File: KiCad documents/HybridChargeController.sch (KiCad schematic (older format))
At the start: 89 parts

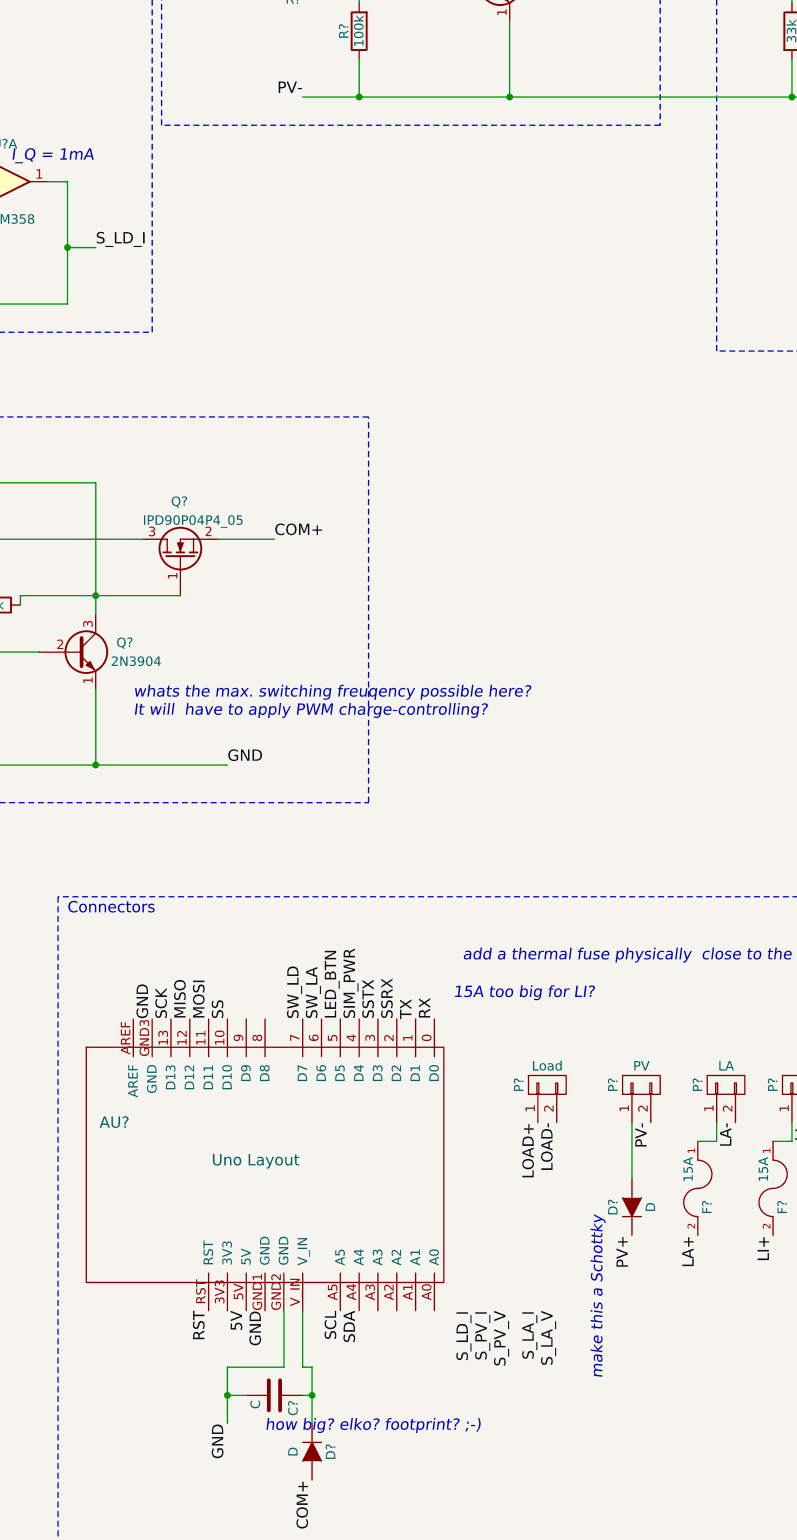
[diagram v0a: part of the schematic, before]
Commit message: added multiplexer
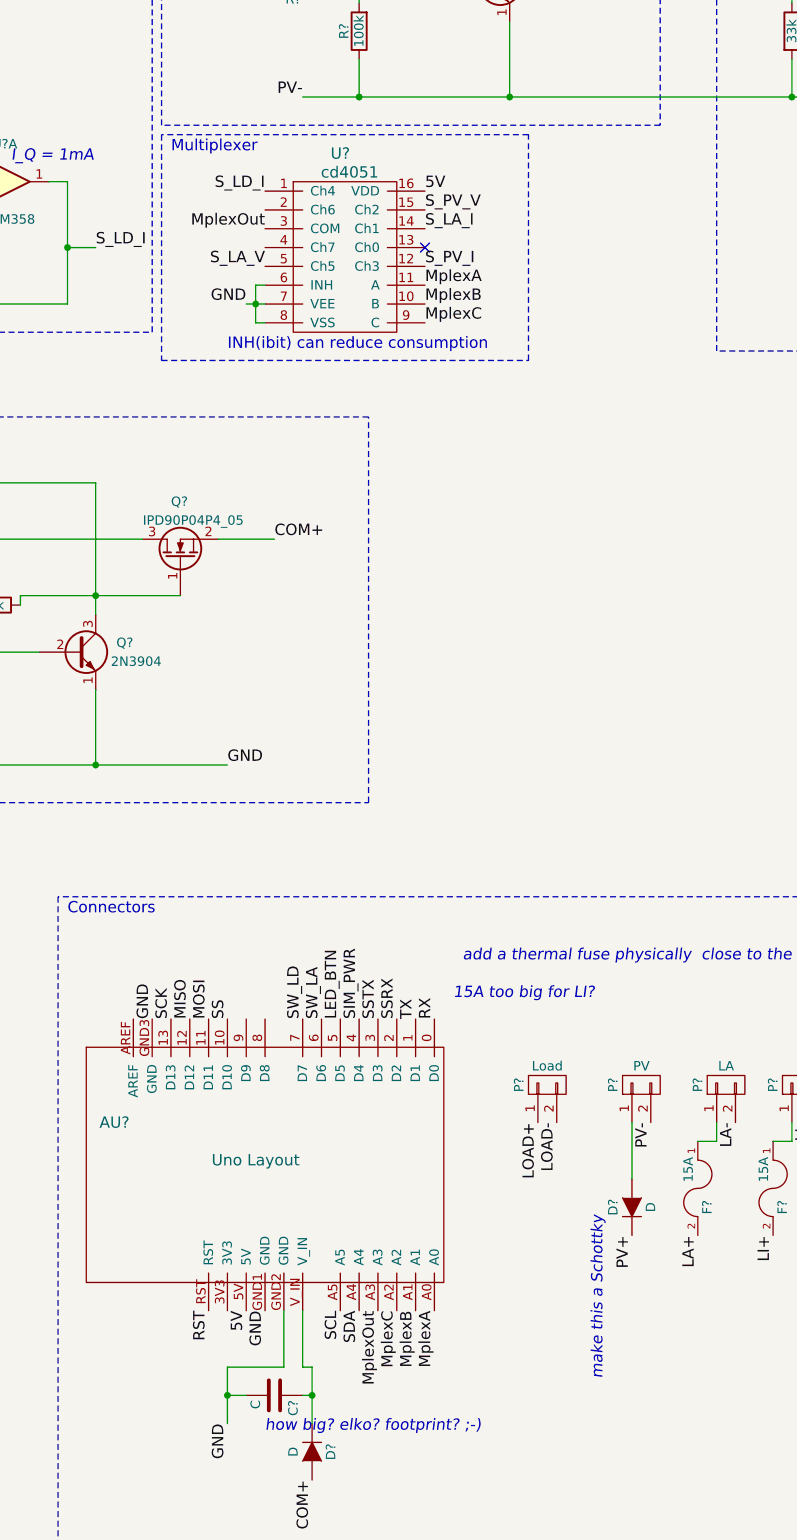
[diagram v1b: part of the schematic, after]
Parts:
- added U?: cd4051, symbol cd4051
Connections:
- net 5V: now also U?.16 (VDD)
- net GND: now also U?.6 (INH), U?.7 (VEE), U?.8 (VSS)
- net S_LA_I: now also U?.14 (Ch1)
- net S_LA_V: now also U?.5 (Ch5)
- net S_LD_I: now also U?.1 (Ch4)
- net S_PV_I: now also U?.12 (Ch3)
- net S_PV_V: now also U?.15 (Ch2)
- net MplexA: now reaches AU?.A0
- net MplexA: now also U?.11 (A)
- net MplexB: now reaches AU?.A1
- net MplexB: now also U?.10 (B)
- net MplexC: now reaches AU?.A2
- net MplexC: now also U?.9 (C)
- net MplexOut: now reaches AU?.A3
- net MplexOut: now also U?.3 (COM)
- no-connect marks 1 -> 2
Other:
- note added: "INH(ibit) can reduce consumption"
- note added: "Multiplexer"
- note removed: "whats the max. switching freuqency possible here? \nIt will have to apply PWM charge-controlling?"

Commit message: added protections
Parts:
- added D? (x2): D, symbol D
- added Q? (x2): Q_PMOS_DGS, symbol Q_PMOS_DGS
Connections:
- wire segments 258 -> 282
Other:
- note added: "10mF?"
- note added: "Connectors & Protection"
- note added: "OR BALANCER"
- note added: "Schottky"
- note added: "protection: \nreverse polarity & short circuit"
- note removed: "15A too big for LI?"
- note removed: "Connectors"
- note removed: "how big? elko? footprint? ;-)"
- note removed: "make this a Schottky"
- moved on the sheet: D?, F?, P?

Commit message: selfmade STL60P4LLF6
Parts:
- removed D? (x2): D, symbol D
- removed F?: 15A, symbol FUSE
- removed P?: LI, symbol CONN_01X02
- removed Q? (x2): Q_PMOS_DGS, symbol Q_PMOS_DGS
- added F?: 15A, symbol FUSE
- added P?: LI, symbol CONN_01X02
- added Q? (x2): STL60P4LLF6, symbol STL60P4LLF6
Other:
- note removed: "OR BALANCER"
- moved on the sheet: F?, P?

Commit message: order ready
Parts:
- removed C? (x3): Cc, symbol C_Small
- removed D? (x2): D, symbol D
- removed D?: ZENER, symbol ZENER
- removed Q?: N FET cheap, symbol Q_NMOS_DGS
- removed R? (x4): Rc, symbol R
- added C2, C3, C4: 1µ, symbol C_Small
- added P4: Extra, symbol CONN_01X07
- added Q4: BSS138, TO_SOT_Packages_SMD:SOT-23, symbol BSS138
- added R2, R3, R4, R5: 100, symbol R
- C1: renamed from C?; value Cc -> 1µ
- C10, C5, C8: renamed from C?; value 0,1µ -> 0.1µ
- C11: renamed from C?; value C -> 10µ
- C9: renamed from C?; value Cf -> 10µ
- D1, D2: renamed from D?; value D -> 1N4148-T
- D3: renamed from D?; value D -> VSB2045Y-M3/54
- Q3, Q5: renamed from Q?; value P FET -> RQ3E100BNTB
- R1: renamed from R?; value Rc -> 100
- R10: renamed from R?; value Rf -> 100
- R16: renamed from R?; value Rsns -> R005
- gave numbers to parts that had none: 66
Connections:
- net CELL12: now also R4.2
- net CELL23: now also R3.2
- net CELL34: now also R2.2
- net CHG: now also Q4.3 (D)
- net COM+: now also Q11.3 (D), Q2.3 (D), R12.2, R40.2
- net GND: now also Q4.1 (G)
- net LI-: now also R5.2
- net MISO: now also P4.2 (P2)
- net MOSI: now also P4.3 (P3)
- net RST: now also P4.7 (P7)
- net SCK: now also P4.1 (P1)
- net S_LD_I: now also U1.7; no longer U1.1
- net VC0: now also C4.2, R5.1
- net VC1: now also C3.2, C4.1, R4.1
- net VC2: now also C2.2, C3.1, R3.1
- net VC3: now also C2.1, R2.1
- net D8: now reaches AU1.8 (D8)
- net D8: now also P4.5 (P5)
- net D9: now reaches AU1.9 (D9)
- net D9: now also P4.6 (P6)
- net at R34.2, R36.1: now also U1.6 (-); no longer U1.2 (-)
- net at R30.2, R32.2: now also U1.5 (+); no longer U1.3 (+)
- net at D1.2 (A), R25.1: now also Q4.2 (S)
- new net D5: P4.4 (P4)
- no-connect marks 2 -> 5
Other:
- note added: "15A max current measuring"
- note added: "maybe wrong schematic"
- note added: "value may change?"
- note removed: "10mF?"
- note removed: "????"
- note removed: "SIZE?\nRf, Cf"
- note removed: "Schottky"
- note removed: "Schottky? Mosfet? Nothing?"
- note removed: "This R needs to be low. 47k doesnt work"
- note removed: "Zener maybe not needed? DATASHEET"
- note removed: "add a thermal fuse physically close to the lifepo?\n"
- note removed: "open:\n- reverse polarity all ports?\n- short-circuit protection all ports?\n- overvoltage?"
- note removed: "sized for which max. current?"
- moved on the sheet: D3, P1, P3

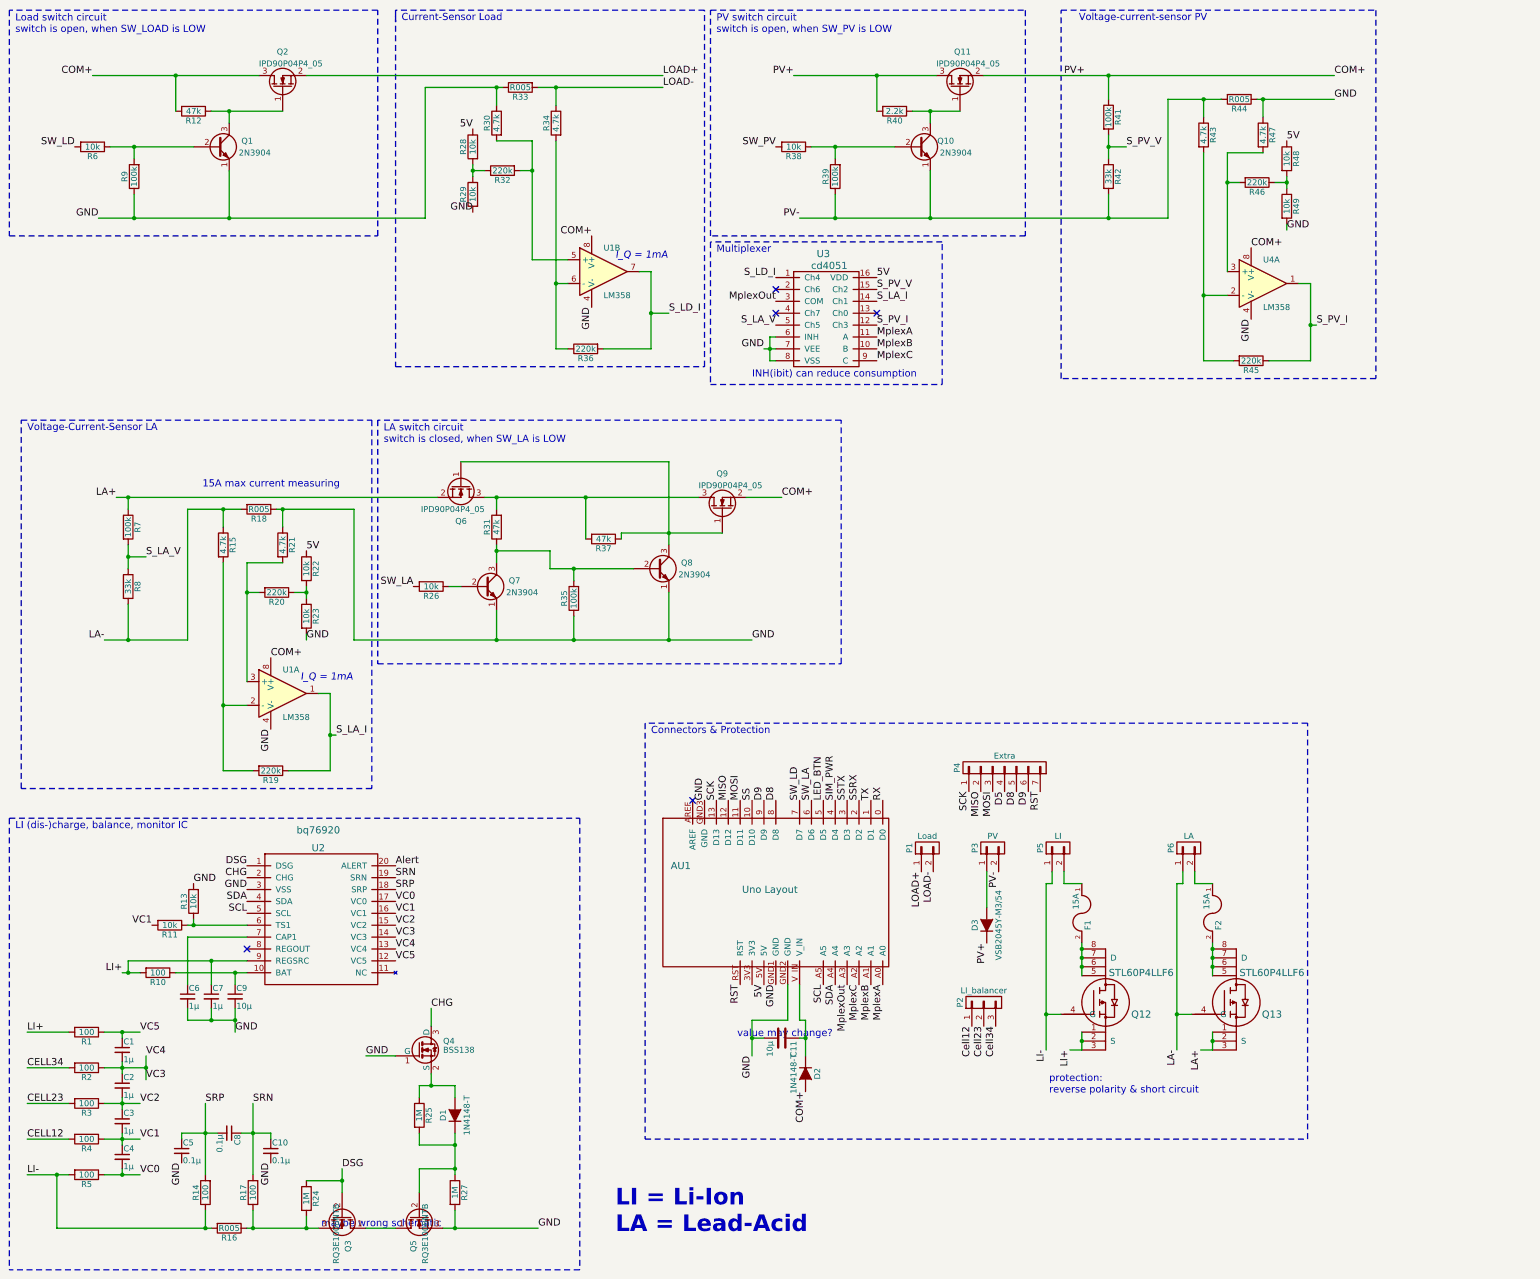
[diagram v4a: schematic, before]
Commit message: added more footprints
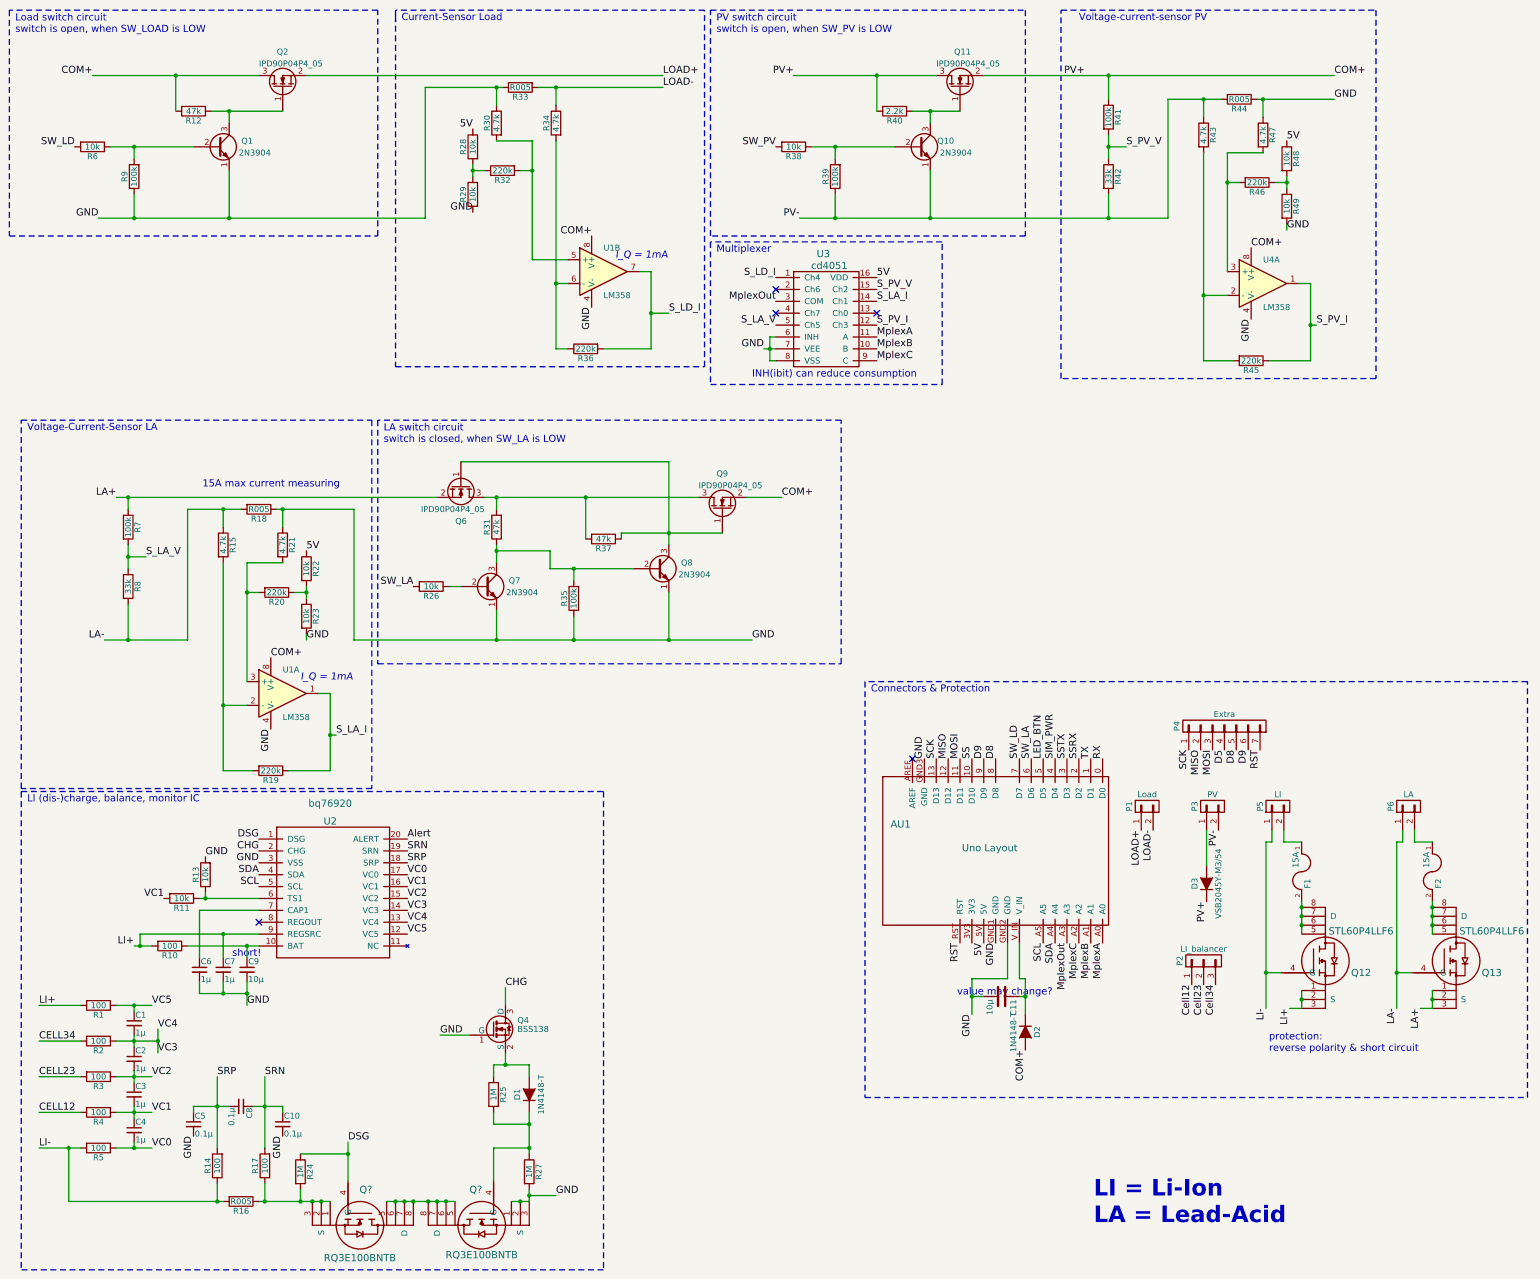
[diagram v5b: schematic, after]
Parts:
- removed Q3, Q5: RQ3E100BNTB, symbol Q_NMOS_DGS
- added Q? (x2): RQ3E100BNTB, bachelorSMDs:HSMT-8, symbol RQ3E100BNTB
- AU1: footprint (none) -> Arduinos:ARDUINO_SHIELD_bigger_holes
- Q12, Q13: footprint (none) -> powerFLAT:powerFLAT_5x6_5..8com
- U2: footprint (none) -> SMD_Packages:SSOP-20
- U3: footprint (none) -> SMD_Packages:SO-16-N
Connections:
- net DSG: now also Q?.4 (G)
- net GND: now also Q?.1, Q?.2 (S), Q?.3
- net at R16.1, R17.1, R24.2: now also Q?.1, Q?.2 (S), Q?.3
- net at D1.1 (K), R25.2, R27.1: now also Q?.4 (G)
- new net: Q?.5, Q?.5, Q?.6, Q?.6, Q?.7 (D), Q?.7 (D), Q?.8, Q?.8
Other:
- note added: "short!"
- note removed: "maybe wrong schematic"
- moved on the sheet: AU1, C1, C10, C11, C2, C3, C4, C5, C6, C7, C8, C9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

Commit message: more and more footprints
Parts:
- removed Q1, Q10, Q7, Q8: 2N3904, symbol Q_NPN_EBC
- removed Q11, Q2, Q6, Q9: IPD90P04P4_05, symbol Q_NMOS_GSD
- added Q1, Q10, Q6, Q8: MMBT3904, TO_SOT_Packages_SMD:SOT-23, symbol Q_NPN_BEC
- added Q11, Q2, Q4, Q9: IPD90P04P4L-04, TO_SOT_Packages_SMD:TO-252-3_TabPin2, symbol IPD90P04P4L-04
- D1, D2: footprint (none) -> Diodes_ThroughHole:D_DO-35_SOD27_P10.16mm_Horizontal
- D3: footprint (none) -> Diodes_ThroughHole:D_P600_R-6_P12.70mm_Horizontal
- P1, P3, P5, P6: footprint (none) -> VCS_library:TerminalBlock_Screw_2pol
- P2: footprint (none) -> Pin_Headers:Pin_Header_Straight_1x03_Pitch2.54mm
- P4: footprint (none) -> Pin_Headers:Pin_Header_Straight_1x07_Pitch2.54mm
- U1, U4: value LM358 -> LM358D; footprint (none) -> SMD_Packages:SOIC-8-N
- gave numbers to parts that had none: 2
- renumbered Q4 to Q7, R6 to R1, R18 to R17, R17 to R18, R1 to R2, R24 to R22, R22 to R23, R23 to R24, R26 to R25, R28 to R26, R29 to R27, R25 to R28, R30 to R29, R2 to R3, R31 to R30, R32 to R31, R33 to R32, R27 to R33, R3 to R4, R4 to R5, R5 to R6
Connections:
- net COM+: now also Q11.2, Q11.3, Q2.3, Q9.2
- net GND: now also Q1.2 (E), Q6.2 (E), Q8.2 (E)
- net LA+: now also Q4.2
- net LOAD+: now also Q2.2
- net PV-: now also Q10.2 (E)
- net at R37.1: now also Q4.1, Q8.3 (C), Q9.1
- net at R30.2, R37.2: now also Q4.3, Q9.3
- net at R30.1, R35.2: now also Q6.3 (C), Q8.1 (B)
- net at R25.1: now also Q6.1 (B)
- net at R12.1: now also Q1.3 (C), Q2.1
- net at R1.1, R9.2: now also Q1.1 (B)
- net at R40.1: now also Q10.3 (C), Q11.1
- net at R38.1, R39.2: now also Q10.1 (B)

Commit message: started pcb
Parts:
- C1, C10, C2, C3, C4, C5, C6, C7, C8: footprint (none) -> Capacitors_SMD:C_0603_HandSoldering
- C11, C9: footprint (none) -> Capacitors_ThroughHole:CP_Radial_D5.0mm_P2.00mm
- F1, F2: footprint (none) -> Fuse_Holders_and_Fuses:Fuse_SMD1206_HandSoldering
- Q12, Q13: footprint powerFLAT:powerFLAT_5x6_5..8com -> bachelorSMDs:powerFLAT_5x6_5..8com
- R1, R10, R11, R12, R13, R14, R15, R18, R19, R2, R20, R21, R22, R23, R24, R25, R26, R27, R28, R29, R3, R30, R31, R33, R34, R35, R36, R37, R38, R39, R4, R40, R41, R42, R43, R45, R46, R47, R48, R49, R5, R6, R7, R8, R9: footprint (none) -> Resistors_SMD:R_0603_HandSoldering
- R16, R17, R32, R44: footprint (none) -> Resistors_SMD:R_1206_HandSoldering
- renumbered U1 to U5
